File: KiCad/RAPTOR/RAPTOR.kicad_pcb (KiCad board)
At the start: 2 copper layers, 101.6 x 55.9 mm, 50 parts, among them J1 SOLC_CONN, J10 EXT_LED3, J11 SRVOL_CONN, J12 SRVOR_CONN, J13 HOTWIRE_CONN, J14 RBF_CONN, J15 EEPROM_BTN_CONN, J16 SOLC_SW_CONN, J17 SOLP_SW_CONN, J18 CONN_BUZZER, J2 SOLP_CONN, J3 JST_2MM_MALE, J4 CONN_LED_FIX, J5 CONN_SOLP_LED, J6 CONN_SOLC_LED, J7 EXT_LED0, J8 EXT_LED1, J9 EXT_LED2, P1 Power, P2 Analog, P3 Digital, P4 Digital, P5 CONN_01X01, P6 CONN_01X01, P7 CONN_01X01, P8 CONN_01X01, Q1 MOSFET-NCH-STQ2NK60ZR-AP, Q2 MOSFET-NCH-STQ2NK60ZR-AP, Q3 MOSFET-NCH-STQ2NK60ZR-AP, Q4 MOSFET-NCH-STQ2NK60ZR-AP, Q5 MOSFET-NCH-STQ2NK60ZR-AP, SW1 SW_Push_Open, SW2 SW_Push_Open, U1 BMP280 Breakout, U2 BNO055 Breakout, U3 OpenLog, U4 AdafruitGPS, U5 U3V12F12, U6 D24V550F5

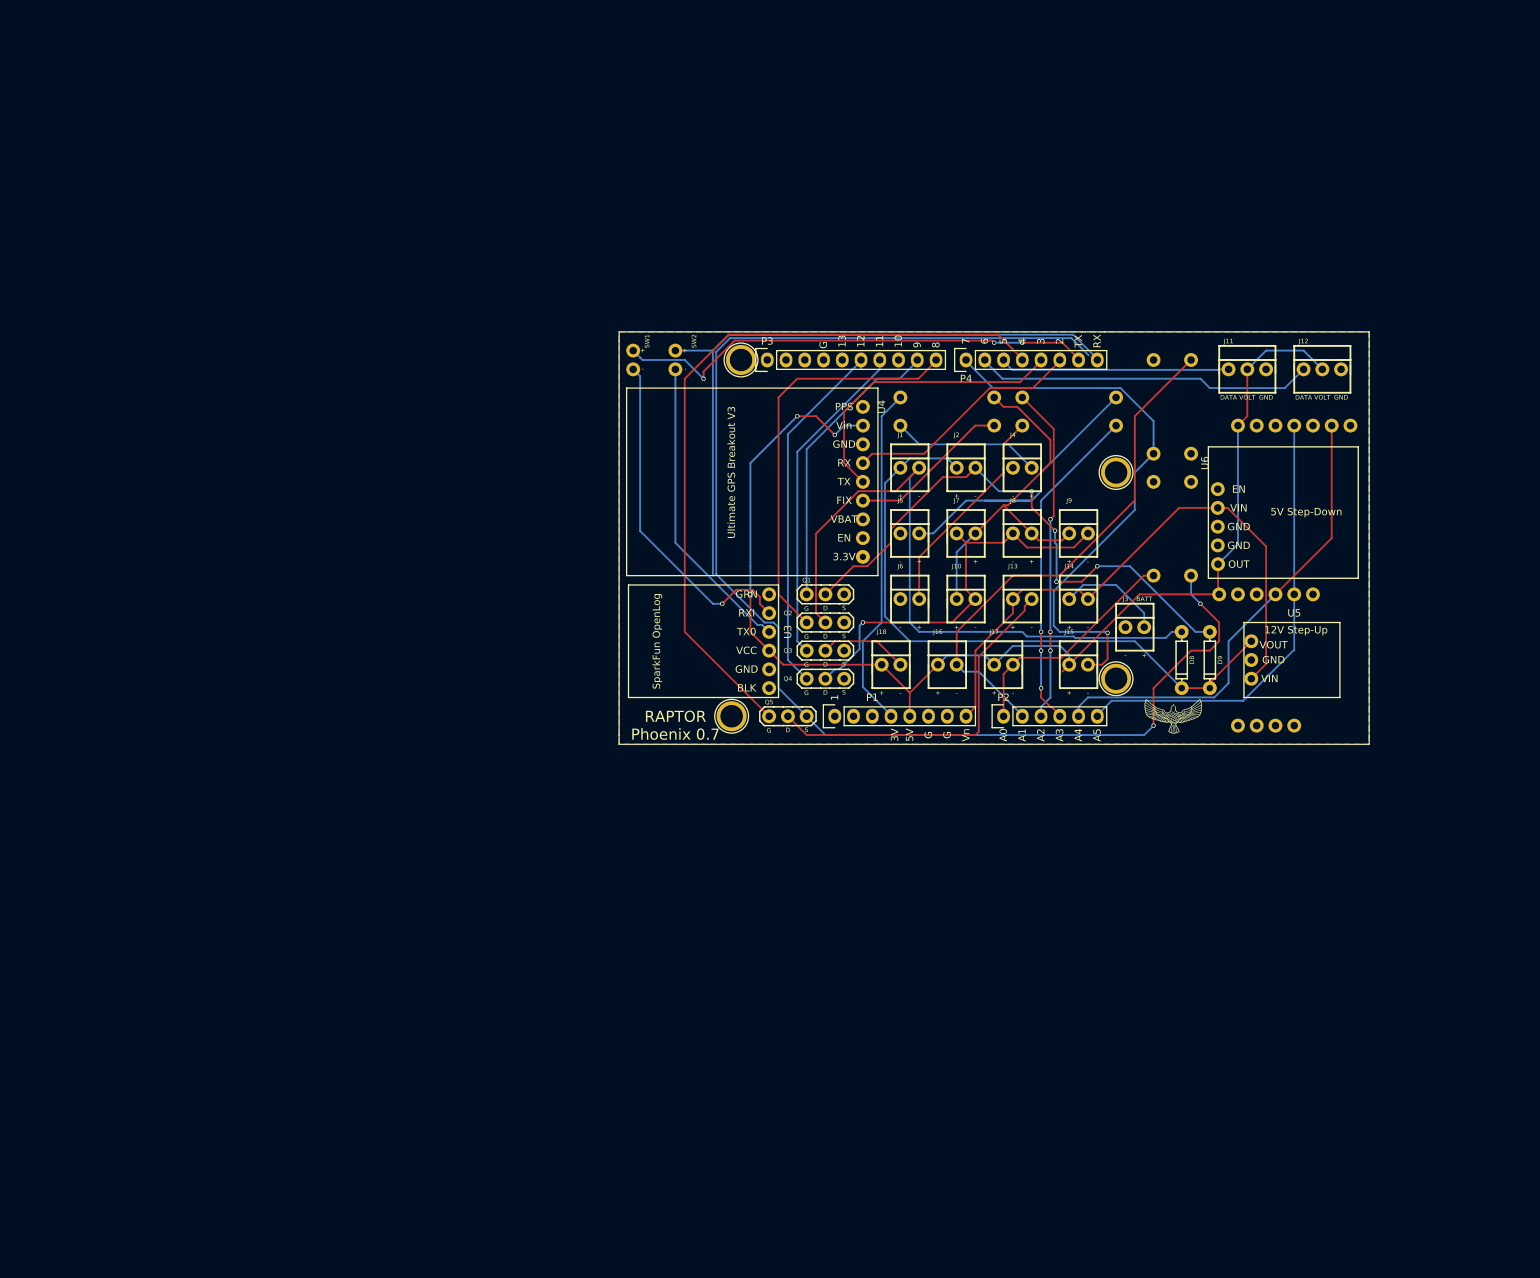
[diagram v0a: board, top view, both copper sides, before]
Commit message: make new pcb, add from netlist, phoenix now in phoenix.kicad_pcb
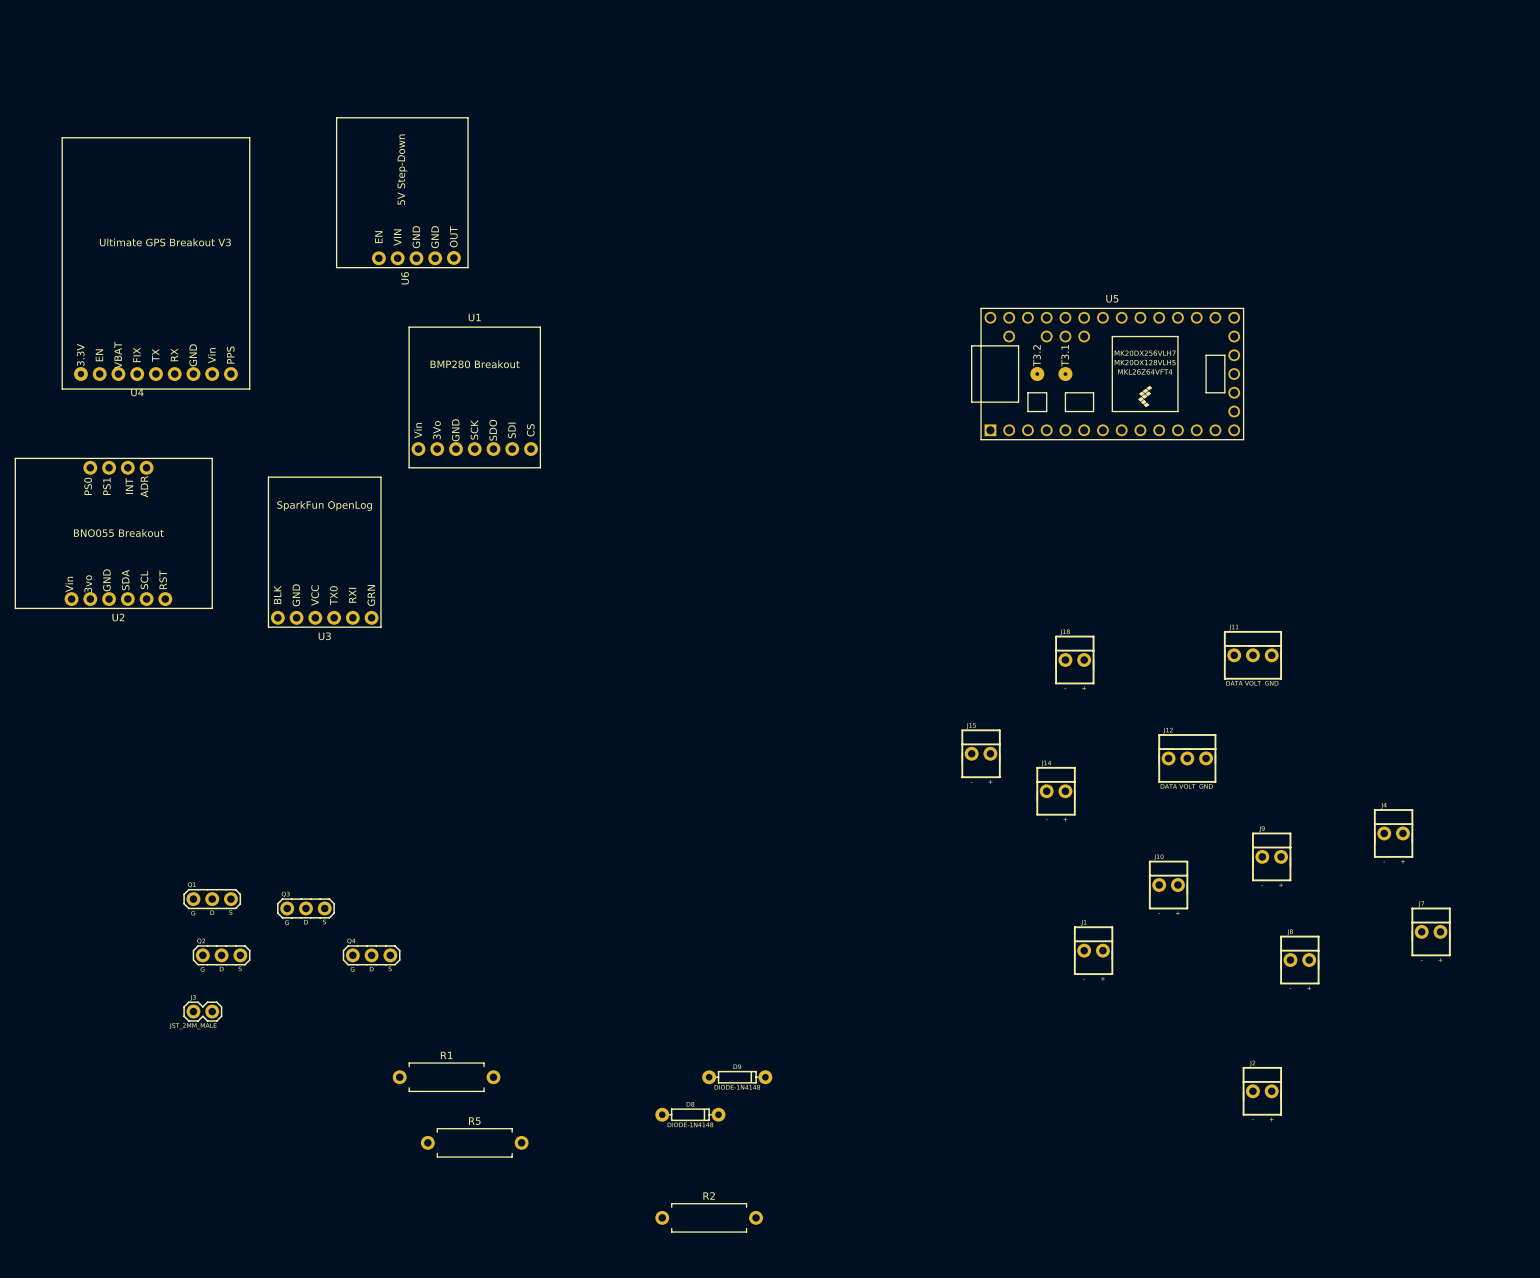
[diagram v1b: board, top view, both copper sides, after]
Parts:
- removed G***: LOGO, RAPTOR_footprints:BirdLogo
- removed J13: HOTWIRE_CONN, RAPTOR_footprints:Molex-2pin
- removed J16: SOLC_SW_CONN, RAPTOR_footprints:Molex-2pin
- removed J17: SOLP_SW_CONN, RAPTOR_footprints:Molex-2pin
- removed J5: CONN_SOLP_LED, RAPTOR_footprints:Molex-2pin
- removed J6: CONN_SOLC_LED, RAPTOR_footprints:Molex-2pin
- removed P1: Power, RAPTOR_footprints:Socket_Strip_Arduino_1x08
- removed P2: Analog, RAPTOR_footprints:Arduino_Analog_06
- removed P3: Digital, RAPTOR_footprints:Arduino_x10_Digital
- removed P4: Digital, RAPTOR_footprints:Arduino_x08_Digital
- removed P5, P6, P7, P8: CONN_01X01, Socket_Arduino_Uno:Arduino_1pin
- removed Q5: MOSFET-NCH-STQ2NK60ZR-AP, RAPTOR_footprints:MOSFET
- removed R3, R4: 100OHM-0603-1_10W-1%, RAPTOR_footprints:Resistor
- removed R6, R7, R8: 4.7KOHM-0603-1_10W-1%, RAPTOR_footprints:Resistor
- removed SW1, SW2: SW_Push_Open, RAPTOR_footprints:Jumper
- J15: value EEPROM_BTN_CONN -> EEP_BTN_CONN
- J3: footprint RAPTOR_footprints:Molex-BATT -> RAPTOR_footprints:2_Pin_Connector
- R1, R2, R5, U1, U2: moved to F.Cu
- U5: value U3V12F12 -> Teensy3.2; footprint RAPTOR_footprints:U3V12F12 -> Teensy_Footprints:Teensy30_31_32_LC
- moved U2 155.4 mm to (41.9, 108.0)
- moved J3 136.3 mm to (52.1, 163.8)
- moved R5 135.6 mm to (83.8, 181.6), turned to 0 degrees
- moved U6 121.4 mm to (73.7, 61.0), turned to 0 degrees
- moved R1 114.4 mm to (80.0, 172.7)
- moved R2 112.1 mm to (115.6, 191.8)
- moved U1 111.0 mm to (90.2, 87.6)
- moved U4 96.9 mm to (47.0, 77.5), turned to 0 degrees
- moved J2 93.5 mm to (195.6, 175.3)
- moved Q2 93.4 mm to (53.3, 156.2)
- moved Q1 92.7 mm to (52.1, 148.6)
- moved D8 90.7 mm to (119.4, 177.8), turned to 0 degrees
- moved D9 85.4 mm to (125.7, 172.7), turned to 0 degrees
- moved J7 83.0 mm to (218.4, 153.7)
- moved Q3 78.5 mm to (64.8, 149.9)
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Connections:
- D8 pad C: +12V -> +7.5V
- D9 pad C: +12V -> +7.5V
- J1 pad 1: +12V -> +7.5V
- J11 pad 1: /SRVO_L -> Net-(J11-Pad1)
- J12 pad 1: /SRVO_R -> Net-(J12-Pad1)
- J15 pad 2: /EEPROM_BTN -> /EEP_BTN
- J2 pad 1: +12V -> +7.5V
- R5 pad 1: /EEPROM_BTN -> /EEP_BTN
- R5 pad 2: GND -> Net-(R5-Pad2)
- U5 pad 1: +12V -> GND
- U5 pad 2: GND -> /SD_RX
- U5 pad 3: +7.5V -> /SD_TX
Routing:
- net Net-(Q5-Pad2): track 182.9 -> 0.00 mm, vias 2 -> 0
- net +5V: track 167.6 -> 0.00 mm, vias 3 -> 0
- net /HOTWIRE: track 100.1 -> 0.00 mm
- net /SD_TX: track 90.0 -> 0.00 mm
- net Net-(D8-PadA): track 89.7 -> 0.00 mm
- net +12V: track 86.4 -> 0.00 mm
- net +7.5V: track 79.9 -> 0.00 mm
- net /EEPROM_BTN: track 76.5 -> 0.00 mm, vias 1 -> 0
- net Net-(D9-PadA): track 76.4 -> 0.00 mm, vias 4 -> 0
- net /SOLC_SW: track 70.2 -> 0.00 mm
- net /SD_RX: track 65.9 -> 0.00 mm, vias 3 -> 0
- net /I2C_SDA: track 63.7 -> 0.00 mm
- net /I2C_SCL: track 60.8 -> 0.00 mm
- net /SOLC_DTA: track 55.6 -> 0.00 mm
- net Net-(J10-Pad2): track 55.2 -> 0.00 mm, vias 1 -> 0
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- removed copper zone on B.Cu, net GND
- removed copper zone on F.Cu, net GND
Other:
- board outline removed
- net class Default: via_dia 0.6 -> 0.8
- board text removed: "1"
- board text removed: "RAPTOR Phoenix 0.7"

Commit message: Manuvered Componets as Such
Made the PCB kinda organzed
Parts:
- J3: value JST_2MM_MALE -> POWER
- Q1, Q2: value MOSFET-NCH-STQ2NK60ZR-AP -> SOLC_MSFT
- Q3: value MOSFET-NCH-STQ2NK60ZR-AP -> BZZ_MSFT
- Q4: value MOSFET-NCH-STQ2NK60ZR-AP -> LED_MSFT
- moved U2 172.2 mm to (209.6, 68.6)
- moved U4 161.5 mm to (199.4, 130.8), turned to 270 degrees
- moved Q3 153.8 mm to (205.7, 88.3)
- moved U3 142.3 mm to (210.8, 106.7), turned to 270 degrees
- moved R5 133.3 mm to (112.4, 51.4), turned to 270 degrees
- moved J2 128.2 mm to (99.7, 90.2)
- moved Q2 101.6 mm to (116.8, 76.8)
- moved Q4 98.0 mm to (160.0, 109.9)
- moved J12 96.8 mm to (127.0, 51.4)
- moved J15 96.3 mm to (100.3, 52.1)
- moved R1 94.6 mm to (165.1, 131.4), turned to 90 degrees
- moved R2 89.5 mm to (182.9, 132.7), turned to 90 degrees
- moved J7 88.2 mm to (137.2, 119.4)
- moved U1 87.5 mm to (175.3, 67.3)
- moved J1 85.3 mm to (118.7, 90.2)
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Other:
- board outline added: 138.4 x 101.6 mm

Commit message: Routed The Headder
Got the pins where I wanted them to make routing easeir
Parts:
- added J5: EXTENSION_HEADER, Connector_IDC:IDC-Header_2x07_P2.54mm_Vertical, F.Cu at (100.1, 97.0)
- J3: value POWER -> JST_2MM_MALE
- Q1, Q2: value SOLC_MSFT -> MOSFET-NCH-STQ2NK60ZR-AP
- Q3: value BZZ_MSFT -> MOSFET-NCH-STQ2NK60ZR-AP
- Q4: value LED_MSFT -> MOSFET-NCH-STQ2NK60ZR-AP
- R1, R2: moved to B.Cu
- moved J18 112.6 mm to (109.7, 78.7)
- moved Q3 96.1 mm to (111.8, 68.1)
- moved U2 72.6 mm to (137.2, 74.2)
- moved Q1 65.0 mm to (162.7, 73.8)
- moved U3 63.9 mm to (166.1, 61.0), turned to 315 degrees
- moved J2 63.8 mm to (163.3, 85.9)
- moved U6 62.4 mm to (175.3, 113.8), turned to 215 degrees
- moved D9 61.8 mm to (165.2, 96.0)
- moved J1 61.8 mm to (180.5, 87.1)
- moved Q2 61.8 mm to (178.6, 73.8)
- moved D8 61.8 mm to (184.3, 96.0)
- moved U4 55.1 mm to (144.8, 123.4), turned to 180 degrees
- moved R1 49.5 mm to (124.5, 103.1), turned to 0 degrees
- moved R2 38.7 mm to (158.5, 102.6), turned to 180 degrees
- moved J4 36.8 mm to (180.3, 104.1)
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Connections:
- J11 pad 1: Net-(J11-Pad1) -> /SRVO_L
- J12 pad 1: Net-(J12-Pad1) -> /SRVO_R
- R5 pad 2: Net-(R5-Pad2) -> GND
- U5 pad 12: Net-(U5-Pad12) -> /PIN_10
- U5 pad 13: Net-(U5-Pad13) -> /PIN_11
- U5 pad 14: Net-(U5-Pad14) -> /PIN_12
- U5 pad 19: Net-(U5-Pad19) -> /PIN_A14
- U5 pad 22: /HOTWIRE -> /PIN_15
- U5 pad 30: Net-(U5-Pad30) -> /PIN_23
- U5 pad 31: Net-(U5-Pad31) -> +3V3
- U5 pad 36: Net-(U5-Pad36) -> /PIN_A10
- U5 pad 37: Net-(U5-Pad37) -> /PIN_A11
- U5 pad 4: Net-(U5-Pad4) -> /PIN_2
- U5 pad 5: Net-(U5-Pad5) -> /PIN_3
- U5 pad 6: Net-(U5-Pad6) -> /PIN_4
- U5 pad 7: Net-(U5-Pad7) -> /PIN_5
- U5 pad 8: Net-(U5-Pad8) -> /PIN_6
- U5 pad 9: Net-(U5-Pad9) -> /PIN_7
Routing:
- net /PIN_15: track 0.00 -> 71.7 mm
- net /PIN_A14: track 0.00 -> 68.4 mm
- net /PIN_11: track 0.00 -> 63.6 mm
- net /PIN_3: track 0.00 -> 62.6 mm
- net /PIN_A10: track 0.00 -> 61.7 mm
- net /PIN_5: track 0.00 -> 61.6 mm
- net /PIN_7: track 0.00 -> 61.1 mm
- net /PIN_12: track 0.00 -> 60.1 mm
- net /PIN_10: track 0.00 -> 54.0 mm
- net /PIN_6: track 0.00 -> 42.8 mm
- net /PIN_4: track 0.00 -> 37.9 mm
- net /PIN_A11: track 0.00 -> 37.7 mm
- net /PIN_23: track 0.00 -> 33.9 mm
- net /PIN_2: track 0.00 -> 33.0 mm
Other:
- board size 138.4 x 101.6 mm -> 101.6 x 101.6 mm

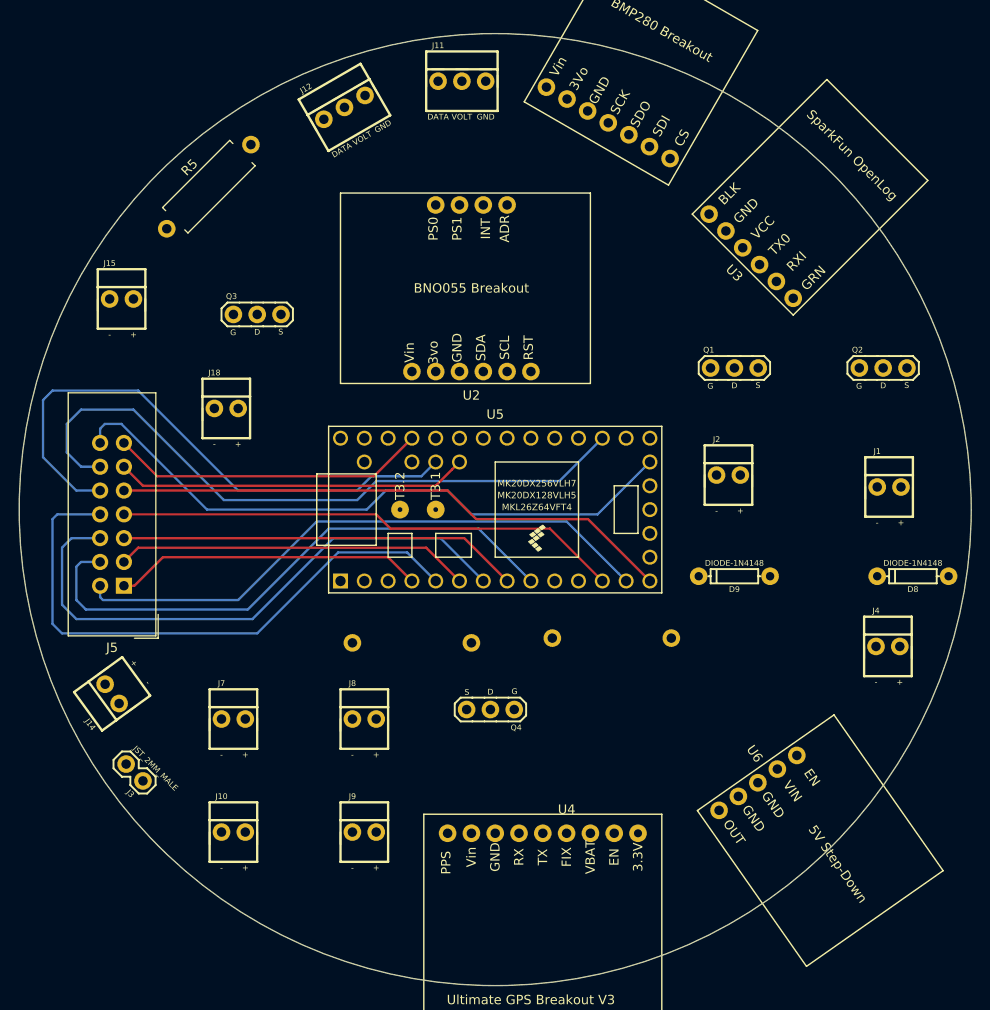
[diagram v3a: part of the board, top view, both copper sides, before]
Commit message: Routed Board no Ground Fill
as seen
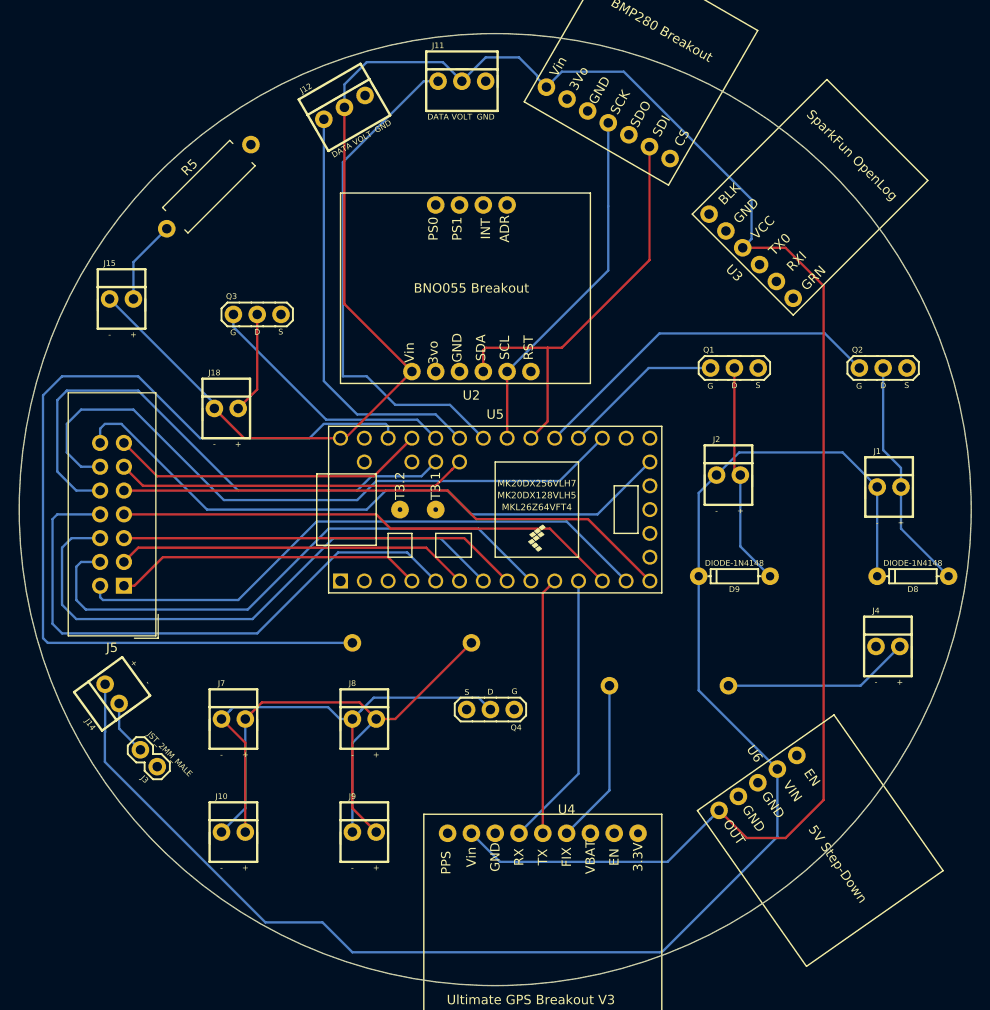
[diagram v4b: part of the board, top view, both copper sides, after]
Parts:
- moved R2 7.94 mm to (164.6, 107.7)
- moved J3 2.16 mm to (103.6, 116.3)
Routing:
- net +5V: track 0.00 -> 244.2 mm
- net +7.5V: track 0.00 -> 165.6 mm
- net +3V3: track 0.00 -> 101.6 mm
- net Net-(J10-Pad2): track 0.00 -> 57.5 mm
- net Net-(J10-Pad1): track 0.00 -> 55.2 mm
- net /SRVO_L: track 0.00 -> 54.3 mm
- net /I2C_SDA: track 0.00 -> 46.5 mm
- net /SRVO_R: track 0.00 -> 44.9 mm
- net /SOLC_DTA: track 0.00 -> 38.7 mm
- net /I2C_SCL: track 0.00 -> 38.5 mm
- net /GPS_RX: track 0.00 -> 29.6 mm
- net /BZZ_DTA: track 0.00 -> 27.8 mm
- net /GPS_TX: track 0.00 -> 27.5 mm
- net Net-(D8-PadA): track 0.00 -> 25.1 mm
- net Net-(D9-PadA): track 0.00 -> 23.8 mm
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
